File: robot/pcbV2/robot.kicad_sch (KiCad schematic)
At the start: 4 parts, among them U1 ESP32_NODEMCU

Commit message: dopisany tekst w latexie
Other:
- moved on the sheet: C3, C7, C8, U1

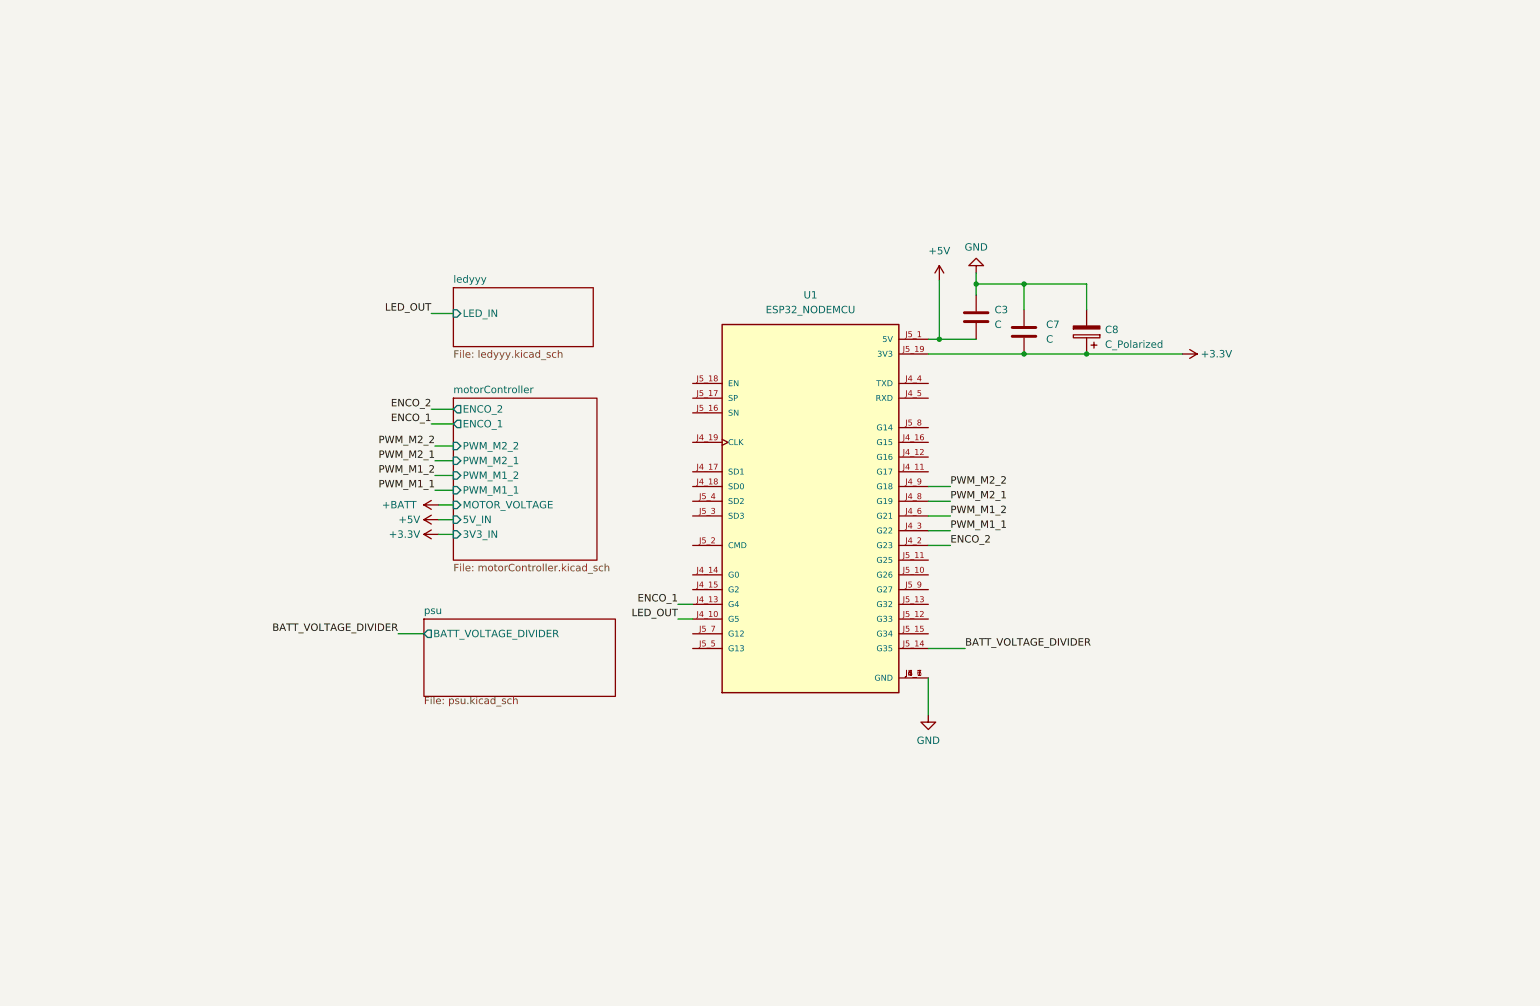
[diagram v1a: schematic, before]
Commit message: uproszczony schemat
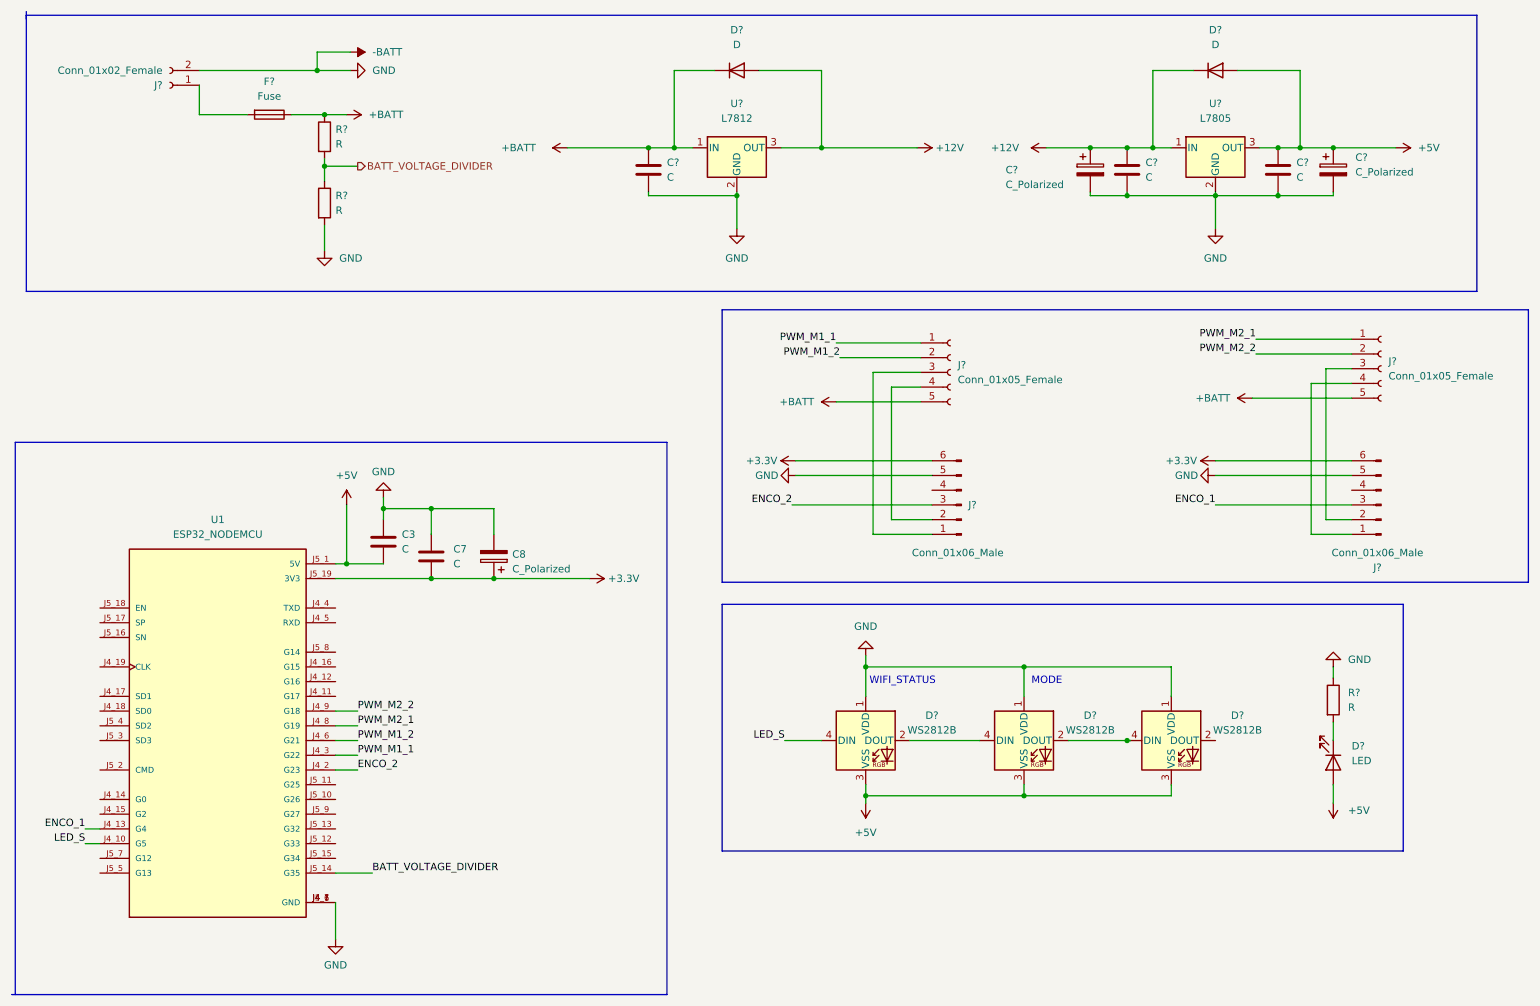
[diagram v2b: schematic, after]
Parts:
- added C? (x3): C, Capacitor_SMD:C_1210_3225Metric, symbol Device:C
- added C? (x2): C_Polarized, Capacitor_SMD:CP_Elec_6.3x7.7, symbol Device:C_Polarized
- added D? (x3): WS2812B, LED_SMD:LED_WS2812B_PLCC4_5.0x5.0mm_P3.2mm, symbol LED:WS2812B
- added D? (x2): D, Diode_SMD:D_1210_3225Metric, symbol Device:D
- added D?: LED, LED_THT:LED_D3.0mm, symbol Device:LED
- added F?: Fuse, Fuse:Fuse_1210_3225Metric_Pad1.42x2.65mm_HandSolder, symbol Device:Fuse
- added J?: Conn_01x02_Female, TerminalBlock:TerminalBlock_bornier-2_P5.08mm, symbol Connector:Conn_01x02_Female
- added J? (x2): Conn_01x05_Female, Connector_Wire:SolderWire-0.75sqmm_1x05_P4.8mm_D1.25mm_OD2.3mm, symbol Connector:Conn_01x05_Female
- added J? (x2): Conn_01x06_Male, Connector_Hirose:Hirose_DF13C_CL535-0406-3-51_1x06-1MP_P1.25mm_Vertical, symbol Connector:Conn_01x06_Male
- added R? (x3): R, Resistor_THT:R_Axial_DIN0207_L6.3mm_D2.5mm_P10.16mm_Horizontal, symbol Device:R
- added U?: L7805, Package_TO_SOT_SMD:TO-252-2, symbol Regulator_Linear:L7805
- added U?: L7812, Package_TO_SOT_THT:TO-220-3_Vertical, symbol Regulator_Linear:L7812
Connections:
- net +3.3V: now also J?.6 (Pin_6), J?.6 (Pin_6)
- net +5V: now also C?.1, C?.1, D?.2 (A), D?.2 (A), D?.3 (VSS), D?.3 (VSS), D?.3 (VSS), U?.3 (OUT)
- net +BATT: now also C?.1, D?.1 (K), F?.1, J?.5 (Pin_5), J?.5 (Pin_5), R?.1, U?.1 (IN)
- net BATT_VOLTAGE_DIVIDER: now also R?.1, R?.2
- net ENCO_1: now also J?.3 (Pin_3)
- net ENCO_2: now also J?.3 (Pin_3)
- net PWM_M1_1: now also J?.1 (Pin_1)
- net PWM_M1_2: now also J?.2 (Pin_2)
- net PWM_M2_1: now also J?.1 (Pin_1)
- net PWM_M2_2: now also J?.2 (Pin_2)
- net GND renamed -BATT
- net -BATT: now also C?.2, C?.2, C?.2, C?.2, C?.2, D?.1 (VDD), D?.1 (VDD), D?.1 (VDD), J?.2 (Pin_2), J?.5 (Pin_5), J?.5 (Pin_5), R?.1, R?.2, U?.2 (GND), U?.2 (GND)
- net LED_OUT renamed LED_S
- net LED_S: now also D?.4 (DIN)
- new net: D?.2 (DOUT), D?.4 (DIN) (x2)
- new net: F?.2, J?.1 (Pin_1)
- new net: J?.1 (Pin_1), J?.3 (Pin_3)
- new net: J?.2 (Pin_2), J?.4 (Pin_4)
- new net: J?.2 (Pin_2), J?.3 (Pin_3)
- new net: J?.1 (Pin_1), J?.4 (Pin_4)
- new net: D?.1 (K), R?.2
- new net +12V: C?.1, C?.1, D?.1 (K), D?.2 (A), U?.1 (IN), U?.3 (OUT)
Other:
- removed sheet ledyyy
- removed sheet motorController
- removed sheet psu
- note added: "MODE"
- note added: "WIFI_STATUS"
- company: (none) -> Damian Bielecki
- title: (none) -> Projekt robotami 
- moved on the sheet: C3, C7, C8, U1
